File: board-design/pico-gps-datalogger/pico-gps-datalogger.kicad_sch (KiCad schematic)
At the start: 23 parts, among them J1 Conn_01x08_Female, J2 Conn_01x09_Female, J3 Conn_01x02_Female, J4 Conn_01x06_Female, SW1 SW_Push, SW2 SW_Push, SW3 SW_Push, SW4 SW_SPDT, SW5 Power Switch, U1 AMS1117-3.3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

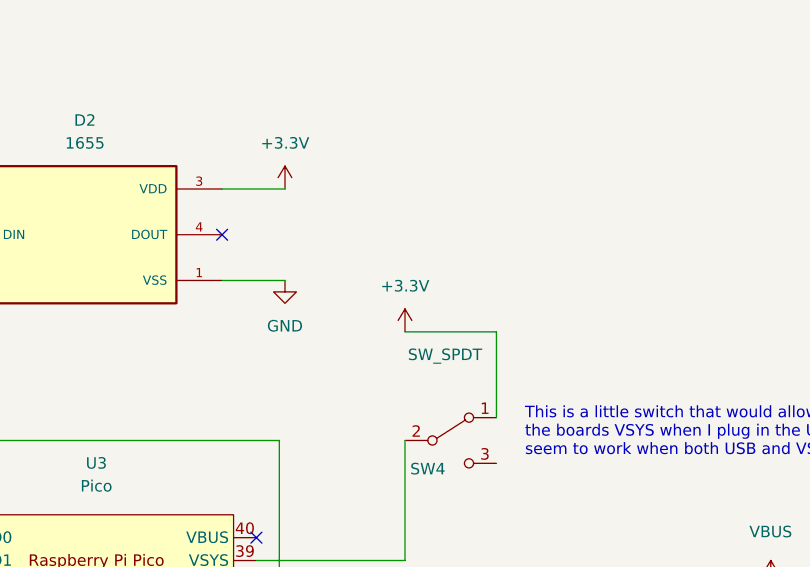
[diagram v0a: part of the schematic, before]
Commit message: updated pcb a bit, to power pico with 5v not 3v3 as it doesn't seem to like that. Added datasheet for GPS.
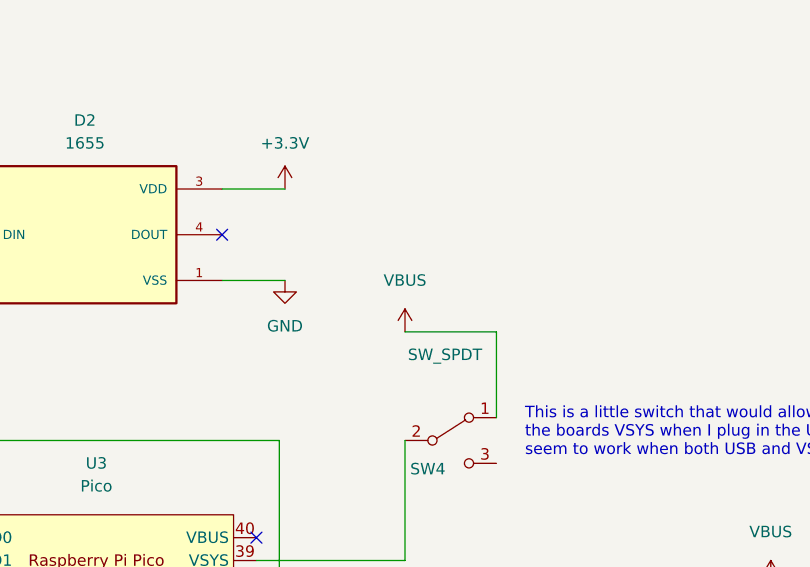
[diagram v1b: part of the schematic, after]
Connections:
- net +3.3V: no longer SW4.1 (A)
- net VBUS: now also SW4.1 (A)
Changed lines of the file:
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@@
     (title "RPI Pico - SPI Display with Neopixel - GPS and SD Card")
     (date "2022-12-28")
-    (rev "0.3")
+    (rev "0.4")
     (company "Mark McGookin")
     (comment 1 "Incremental Board for development")
     (comment 2 "Added SD Card pinouts and GPS footprint")
+    (comment 3 "Fixed power to board. 5v now not 3v3")
   )
   (junction (at 35.56 55.88) (diameter 0) (color 0 0 0 0)
@@
     (pin "1")
   )
-  (symbol (lib_id "power:+3.3V") (at 192.405 52.705 0) (unit 1)
-    (in_bom yes) (on_board yes) (fields_autoplaced)
-    (property "Reference" "#PWR014" (id 0) (at 192.405 56.515 0)
-      (effects (font (size 1.27 1.27)) hide)
-    )
-    (property "Value" "+3.3V" (id 1) (at 192.405 47.625 0))
-    (property "Footprint" "" (id 2) (at 192.405 52.705 0)
-      (effects (font (size 1.27 1.27)) hide)
-    )
-    (property "Datasheet" "" (id 3) (at 192.405 52.705 0)
-      (effects (font (size 1.27 1.27)) hide)
-    )
-    (pin "1")
-  )
   (symbol (lib_id "power:VBUS") (at 24.765 26.67 0) (unit 1)
     (in_bom yes) (on_board yes) (fields_autoplaced)
@@
     (pin "1")
   )
+  (symbol (lib_id "power:VBUS") (at 192.405 52.705 0) (unit 1)
+    (in_bom yes) (on_board yes) (fields_autoplaced)
+    (property "Reference" "#PWR0101" (id 0) (at 192.405 56.515 0)
+      (effects (font (size 1.27 1.27)) hide)
+    )
+    (property "Value" "VBUS" (id 1) (at 192.405 46.99 0))
+    (property "Footprint" "" (id 2) (at 192.405 52.705 0)
+      (effects (font (size 1.27 1.27)) hide)
+    )
+    (property "Datasheet" "" (id 3) (at 192.405 52.705 0)
+      (effects (font (size 1.27 1.27)) hide)
+    )
+    (pin "1")
+  )
   (symbol (lib_id "Connector:Conn_01x08_Female") (at 101.6 90.805 180) (unit 1)
     (in_bom yes) (on_board yes) (fields_autoplaced)
@@
       (reference "#PWR013") (unit 1) (value "GND") (footprint "")
     )
-    (path "/1b6001ca-a9dd-470b-bac3-68a19915bebc"
-      (reference "#PWR014") (unit 1) (value "+3.3V") (footprint "")
-    )
     (path "/b4615784-a348-46bf-be0a-a96c7aeacf33"
       (reference "#PWR015") (unit 1) (value "VBUS") (footprint "")
@@
       (reference "#PWR016") (unit 1) (value "GND") (footprint "")
     )
+    (path "/6113a20f-0551-4d08-8eb3-c085f12c0a6f"
+      (reference "#PWR0101") (unit 1) (value "VBUS") (footprint "")
+    )
     (path "/05a4009a-7485-4cda-964e-1e4baabf6d92"
